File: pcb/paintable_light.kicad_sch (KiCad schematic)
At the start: 19 parts, among them J2 Conn_01x02, J3 Conn_02x03_Odd_Even, U1 WS2811, U2 WS2811, U3 ATtiny85-20P

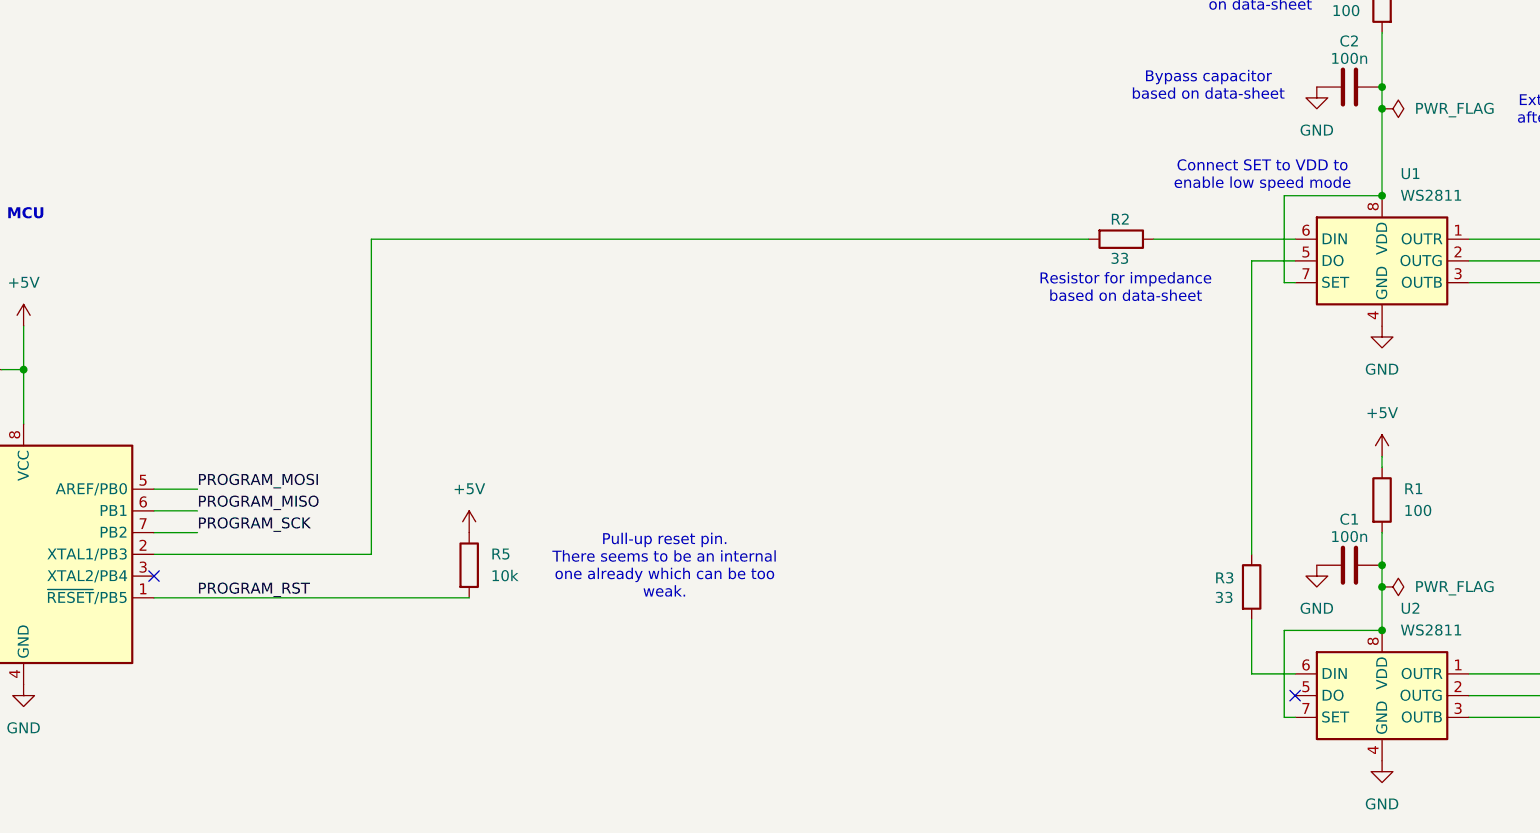
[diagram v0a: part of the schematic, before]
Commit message: enable high speed
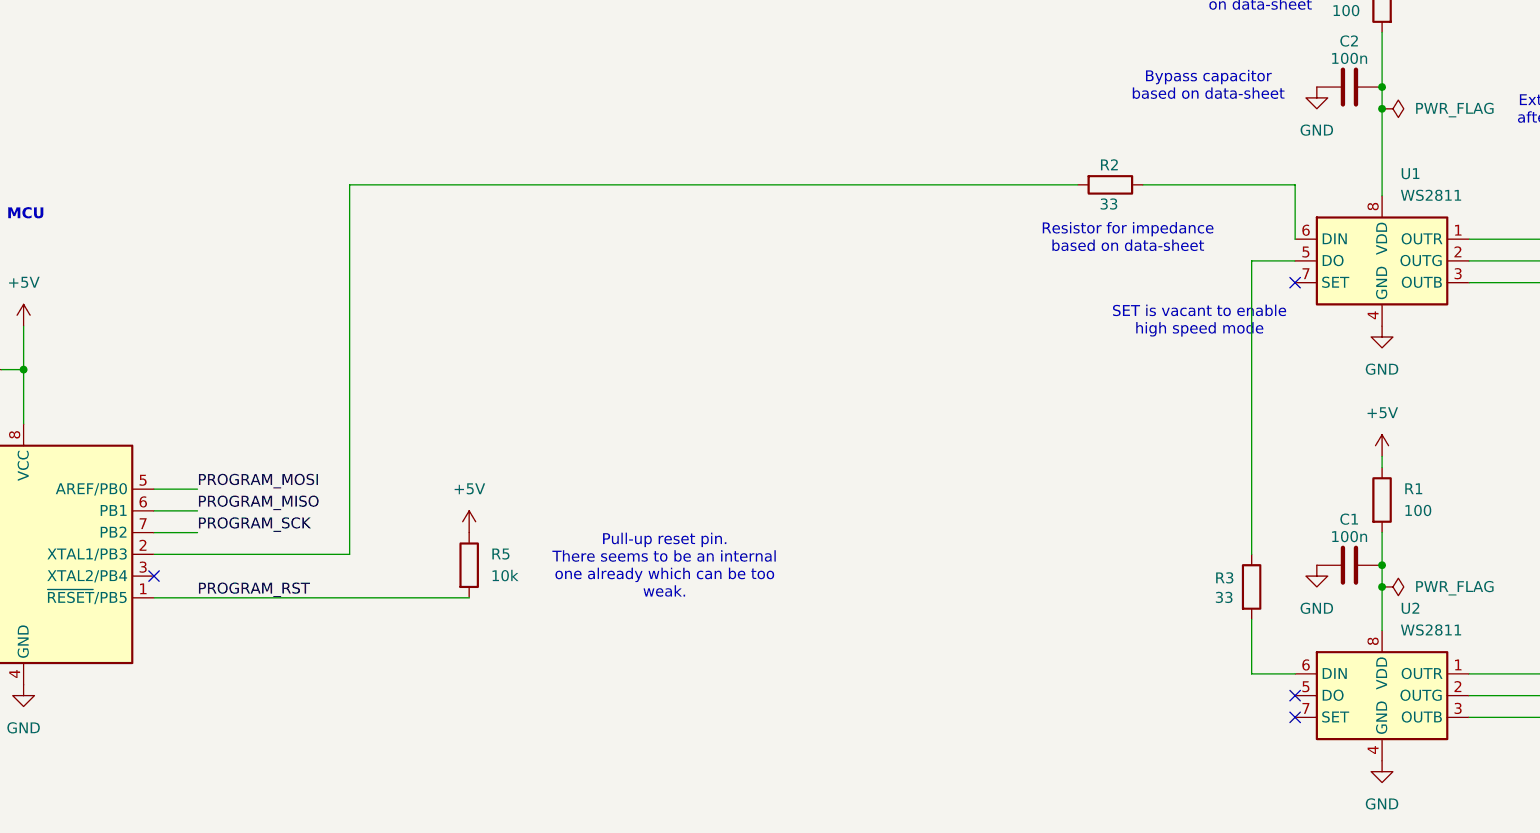
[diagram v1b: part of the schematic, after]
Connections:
- net at C2.2, R4.2, U1.8 (VDD): no longer U1.7 (SET)
- net at C1.2, R1.2, U2.8 (VDD): no longer U2.7 (SET)
- no-connect marks 2 -> 4
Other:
- note added: "SET is vacant to enable high speed mode"
- note removed: "Connect SET to VDD to enable low speed mode"
- moved on the sheet: R2
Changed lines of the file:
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@@
 		)
 	)
-	(text "Bypass capacitor"
+	(text "SET is vacant to enable\nhigh speed mode"
 		(exclude_from_sim no)
-		(at 40.132 98.552 0)
+		(at 195.834 94.742 0)
 		(effects
 			(font
@@
 		)
 	)
-	(text "MCU"
+	(text "Bypass capacitor"
 		(exclude_from_sim no)
-		(at 58.674 82.296 0)
+		(at 40.132 98.552 0)
 		(effects
 			(font
 				(size 1.27 1.27)
-				(thickness 0.254)
-				(bold yes)
 			)
 		)
 	)
-	(text "Resistor for impedance\nbased on data-sheet"
+	(text "MCU"
 		(exclude_from_sim no)
-		(at 187.198 90.932 0)
+		(at 58.674 82.296 0)
 		(effects
 			(font
 				(size 1.27 1.27)
+				(thickness 0.254)
+				(bold yes)
 			)
 		)
 	)
-	(text "Connect SET to VDD to \nenable low speed mode"
+	(text "Resistor for impedance\nbased on data-sheet"
 		(exclude_from_sim no)
-		(at 203.2 77.724 0)
+		(at 187.452 85.09 0)
 		(effects
 			(font
@@
 	)
 	(junction
-		(at 217.17 130.81)
-		(diameter 0)
-		(color 0 0 0 0)
-	)
-	(junction
 		(at 217.17 69.85)
 		(diameter 0)
@@
 	)
 	(junction
-		(at 217.17 80.01)
-		(diameter 0)
-		(color 0 0 0 0)
-	)
-	(junction
 		(at 80.01 34.29)
 		(diameter 0)
@@
 	)
 	(no_connect
+		(at 207.01 140.97)
+	)
+	(no_connect
 		(at 207.01 138.43)
 	)
@@
 		(at 73.66 124.46)
 	)
+	(no_connect
+		(at 207.01 90.17)
+	)
 	(wire
 		(pts
@@
 	(wire
 		(pts
-			(xy 217.17 50.8) (xy 217.17 53.34)
+			(xy 207.01 78.74) (xy 207.01 85.09)
 		)
 		(stroke
@@
 	(wire
 		(pts
-			(xy 73.66 121.92) (xy 99.06 121.92)
+			(xy 189.23 78.74) (xy 207.01 78.74)
 		)
 		(stroke
@@
 	(wire
 		(pts
-			(xy 58.42 95.25) (xy 58.42 100.33)
+			(xy 217.17 50.8) (xy 217.17 53.34)
 		)
 		(stroke
@@
 	(wire
 		(pts
-			(xy 236.22 82.55) (xy 241.3 82.55)
+			(xy 73.66 121.92) (xy 96.52 121.92)
 		)
 		(stroke
@@
 	(wire
 		(pts
-			(xy 99.06 121.92) (xy 99.06 85.09)
+			(xy 58.42 95.25) (xy 58.42 100.33)
 		)
 		(stroke
@@
 	(wire
 		(pts
-			(xy 236.22 143.51) (xy 236.22 140.97)
+			(xy 236.22 82.55) (xy 241.3 82.55)
 		)
 		(stroke
@@
 	(wire
 		(pts
-			(xy 217.17 67.31) (xy 217.17 69.85)
+			(xy 96.52 121.92) (xy 96.52 78.74)
 		)
 		(stroke
@@
 	(wire
 		(pts
-			(xy 58.42 100.33) (xy 58.42 106.68)
+			(xy 236.22 143.51) (xy 236.22 140.97)
 		)
 		(stroke
@@
 	(wire
 		(pts
-			(xy 248.92 143.51) (xy 257.81 143.51)
+			(xy 217.17 67.31) (xy 217.17 69.85)
 		)
 		(stroke
@@
 	(wire
 		(pts
-			(xy 248.92 82.55) (xy 257.81 82.55)
+			(xy 58.42 100.33) (xy 58.42 106.68)
 		)
 		(stroke
@@
 	(wire
 		(pts
-			(xy 201.93 129.54) (xy 201.93 135.89)
+			(xy 248.92 143.51) (xy 257.81 143.51)
 		)
 		(stroke
@@
 	(wire
 		(pts
-			(xy 201.93 87.63) (xy 201.93 121.92)
+			(xy 248.92 82.55) (xy 257.81 82.55)
 		)
 		(stroke
@@
 	(wire
 		(pts
-			(xy 257.81 82.55) (xy 257.81 87.63)
+			(xy 201.93 129.54) (xy 201.93 135.89)
 		)
 		(stroke
@@
 	(wire
 		(pts
-			(xy 207.01 140.97) (xy 205.74 140.97)
+			(xy 201.93 87.63) (xy 201.93 121.92)
 		)
 		(stroke
@@
 	(wire
 		(pts
-			(xy 205.74 80.01) (xy 217.17 80.01)
+			(xy 257.81 82.55) (xy 257.81 87.63)
 		)
 		(stroke
@@
 	(wire
 		(pts
-			(xy 205.74 130.81) (xy 217.17 130.81)
-		)
-		(stroke
-			(width 0)
-			(type default)
-		)
-	)
-	(wire
-		(pts
 			(xy 236.22 85.09) (xy 236.22 82.55)
 		)
@@
 	(wire
 		(pts
-			(xy 99.06 85.09) (xy 182.88 85.09)
+			(xy 96.52 78.74) (xy 181.61 78.74)
 		)
 		(stroke
@@
 	(wire
 		(pts
-			(xy 207.01 90.17) (xy 205.74 90.17)
-		)
-		(stroke
-			(width 0)
-			(type default)
-		)
-	)
-	(wire
-		(pts
 			(xy 80.01 36.83) (xy 80.01 34.29)
 		)
@@
 	(wire
 		(pts
-			(xy 205.74 90.17) (xy 205.74 80.01)
-		)
-		(stroke
-			(width 0)
-			(type default)
-		)
-	)
-	(wire
-		(pts
 			(xy 80.01 31.75) (xy 62.23 31.75)
 		)
@@
 	(wire
 		(pts
-			(xy 205.74 140.97) (xy 205.74 130.81)
-		)
-		(stroke
-			(width 0)
-			(type default)
-		)
-	)
-	(wire
-		(pts
 			(xy 73.66 116.84) (xy 78.74 116.84)
 		)
@@
 	(wire
 		(pts
-			(xy 190.5 85.09) (xy 207.01 85.09)
-		)
-		(stroke
-			(width 0)
-			(type default)
-		)
-	)
-	(wire
-		(pts
 			(xy 227.33 138.43) (xy 241.3 138.43)
 		)
@@
 	(symbol
 		(lib_id "Device:R")
-		(at 186.69 85.09 270)
+		(at 185.42 78.74 270)
 		(unit 1)
 		(exclude_from_sim no)
@@
 		(dnp no)
 		(property "Reference" "R2"
-			(at 185.42 82.804 90)
+			(at 184.15 76.454 90)
 			(effects
 				(font
@@
 		)
 		(property "Value" "33"
-			(at 185.42 87.376 90)
+			(at 184.15 81.026 90)
 			(effects
 				(font
@@
 		)
 		(property "Footprint" "Resistor_SMD:R_0603_1608Metric_Pad0.98x0.95mm_HandSolder"
-			(at 186.69 83.312 90)
+			(at 185.42 76.962 90)
 			(effects
 				(font
@@
 		)
 		(property "Datasheet" "~"
-			(at 186.69 85.09 0)
+			(at 185.42 78.74 0)
 			(effects
 				(font
@@
 		)
 		(property "Description" "Resistor"
-			(at 186.69 85.09 0)
+			(at 185.42 78.74 0)
 			(effects
 				(font

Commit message: initial new board layout
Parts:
- removed J2: Conn_01x02, Connector_PinHeader_2.54mm:PinHeader_1x02_P2.54mm_Vertical, symbol Connector_Generic:Conn_01x02
- removed J3: Conn_02x03_Odd_Even, Connector_PinHeader_2.54mm:PinHeader_2x03_P2.54mm_Vertical, symbol Connector_Generic:Conn_02x03_Odd_Even
- removed U3: ATtiny85-20P, Package_DIP:DIP-8_W7.62mm, symbol MCU_Microchip_ATtiny:ATtiny85-20P
- added C3: 100n, Capacitor_SMD:C_1206_3216Metric_Pad1.33x1.80mm_HandSolder, symbol Device:C
- added D7, D8, D9: LED, LED_SMD:LED_0603_1608Metric_Pad1.05x0.95mm_HandSolder, symbol Device:LED
- added J1: Conn_01x03_Pin, Connector_PinHeader_2.54mm:PinHeader_1x03_P2.54mm_Vertical_SMD_Pin1Left, symbol Connector:Conn_01x03_Pin
- added J2, J3: Conn_01x01, TestPoint:TestPoint_Pad_2.5x2.5mm, symbol Connector_Generic:Conn_01x01
- added R6: 100, Resistor_SMD:R_1206_3216Metric_Pad1.30x1.75mm_HandSolder, symbol Device:R
- added U3: WS2811, Package_SO:SOIC-8_3.9x4.9mm_P1.27mm, symbol Driver_LED:WS2811
- added U4: CH32V003JxMx, Package_SO:JEITA_SOIC-8_3.9x4.9mm_P1.27mm, symbol MCU_WCH_RiscV:CH32V003JxMx
- C1: renamed from C2; footprint Capacitor_SMD:C_0603_1608Metric_Pad1.08x0.95mm_HandSolder -> Capacitor_SMD:C_1206_3216Metric_Pad1.33x1.80mm_HandSolder
- C2: renamed from C1; footprint Capacitor_SMD:C_0603_1608Metric_Pad1.08x0.95mm_HandSolder -> Capacitor_SMD:C_1206_3216Metric_Pad1.33x1.80mm_HandSolder
- C4: renamed from C3; footprint Capacitor_SMD:C_0603_1608Metric_Pad1.08x0.95mm_HandSolder -> Capacitor_SMD:C_1206_3216Metric_Pad1.33x1.80mm_HandSolder
- D1, D2, D3: footprint LED_SMD:LED_0603_1608Metric_Pad1.05x0.95mm_HandSolder -> LED_THT:LED_D5.0mm
- R1: renamed from R2; footprint Resistor_SMD:R_0603_1608Metric_Pad0.98x0.95mm_HandSolder -> Resistor_SMD:R_1206_3216Metric_Pad1.30x1.75mm_HandSolder
- R2: renamed from R4; footprint Resistor_SMD:R_0603_1608Metric_Pad0.98x0.95mm_HandSolder -> Resistor_SMD:R_1206_3216Metric_Pad1.30x1.75mm_HandSolder
- R3: footprint Resistor_SMD:R_0603_1608Metric_Pad0.98x0.95mm_HandSolder -> Resistor_SMD:R_1206_3216Metric_Pad1.30x1.75mm_HandSolder
- R4: renamed from R1; footprint Resistor_SMD:R_0603_1608Metric_Pad0.98x0.95mm_HandSolder -> Resistor_SMD:R_1206_3216Metric_Pad1.30x1.75mm_HandSolder
- R5: value 10k -> 33; footprint Resistor_SMD:R_0603_1608Metric_Pad0.98x0.95mm_HandSolder -> Resistor_SMD:R_1206_3216Metric_Pad1.30x1.75mm_HandSolder
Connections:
- net +5V: now also D7.2 (A), D8.2 (A), D9.2 (A), J1.1 (Pin_1), J2.1 (Pin_1), R6.1, U4.4 (VDD); no longer R5.1
- net GND: now also C3.1, J1.3 (Pin_3), J3.1 (Pin_1), U3.4 (GND), U4.2 (VSS)
- net at U1.6 (DIN): now also R1.2; no longer R1.1
- net at U2.5 (DO): now also R5.1
- net PROGRAM_RST: no longer names the net of R5.2
- net PROGRAM_RST: now also U3.6 (DIN)
- new net: D7.1 (K), U3.1 (OUTR)
- new net: D8.1 (K), U3.2 (OUTG)
- new net: D9.1 (K), U3.3 (OUTB)
- new net: C3.2, R6.2, U3.8 (VDD)
- new net LED Signal: R1.1, U4.5 (PC1)
- new net SWDIO: J1.2 (Pin_2), U4.8 (PD1/PD4/PD5)
- no-connect marks 4 -> 8
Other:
- note added: "0603 LEDs"
- note added: "1210 LEDs"
- note added: "Power supply and programming"
- note added: "Solder pads for power"
- note added: "Through hole LEDs"
- note removed: "Connector for programming the MCU"
- note removed: "Pull-up reset pin. There seems to be an internal one already which can be too weak."
- note removed: "Standard Power Supply"
- moved on the sheet: C1, C2, C4, D1, D2, D3, D4, D5, D6, R1, R2, R3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

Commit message: progress
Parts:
- D1, D2, D3: footprint LED_THT:LED_D5.0mm -> front_leds:LED_1210_3225Metric_Pad1.42x2.65mm_HandSolder_front
- D4, D5, D6: footprint LED_SMD:LED_1210_3225Metric_Pad1.42x2.65mm_HandSolder -> front_leds:LED_1210_3225Metric_Pad1.42x2.65mm_HandSolder_front
- D7, D8, D9: footprint LED_SMD:LED_0603_1608Metric_Pad1.05x0.95mm_HandSolder -> front_leds:LED_1210_3225Metric_Pad1.42x2.65mm_HandSolder_front
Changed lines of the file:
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@@
 			)
 		)
-		(property "Footprint" "LED_SMD:LED_0603_1608Metric_Pad1.05x0.95mm_HandSolder"
+		(property "Footprint" "front_leds:LED_1210_3225Metric_Pad1.42x2.65mm_HandSolder_front"
 			(at 156.21 157.48 0)
 			(effects
@@
 			)
 		)
-		(property "Footprint" "LED_SMD:LED_1210_3225Metric_Pad1.42x2.65mm_HandSolder"
+		(property "Footprint" "front_leds:LED_1210_3225Metric_Pad1.42x2.65mm_HandSolder_front"
 			(at 156.21 116.84 0)
 			(effects
@@
 			)
 		)
-		(property "Footprint" "LED_THT:LED_D5.0mm"
+		(property "Footprint" "front_leds:LED_1210_3225Metric_Pad1.42x2.65mm_HandSolder_front"
 			(at 156.21 66.04 0)
 			(effects
@@
 			)
 		)
-		(property "Footprint" "LED_THT:LED_D5.0mm"
+		(property "Footprint" "front_leds:LED_1210_3225Metric_Pad1.42x2.65mm_HandSolder_front"
 			(at 156.21 71.12 0)
 			(effects
@@
 			)
 		)
-		(property "Footprint" "LED_THT:LED_D5.0mm"
+		(property "Footprint" "front_leds:LED_1210_3225Metric_Pad1.42x2.65mm_HandSolder_front"
 			(at 156.21 76.2 0)
 			(effects
@@
 			)
 		)
-		(property "Footprint" "LED_SMD:LED_1210_3225Metric_Pad1.42x2.65mm_HandSolder"
+		(property "Footprint" "front_leds:LED_1210_3225Metric_Pad1.42x2.65mm_HandSolder_front"
 			(at 156.21 111.76 0)
 			(effects
@@
 			)
 		)
-		(property "Footprint" "LED_SMD:LED_0603_1608Metric_Pad1.05x0.95mm_HandSolder"
+		(property "Footprint" "front_leds:LED_1210_3225Metric_Pad1.42x2.65mm_HandSolder_front"
 			(at 156.21 167.64 0)
 			(effects
@@
 			)
 		)
-		(property "Footprint" "LED_SMD:LED_0603_1608Metric_Pad1.05x0.95mm_HandSolder"
+		(property "Footprint" "front_leds:LED_1210_3225Metric_Pad1.42x2.65mm_HandSolder_front"
 			(at 156.21 162.56 0)
 			(effects
@@
 			)
 		)
-		(property "Footprint" "LED_SMD:LED_1210_3225Metric_Pad1.42x2.65mm_HandSolder"
+		(property "Footprint" "front_leds:LED_1210_3225Metric_Pad1.42x2.65mm_HandSolder_front"
 			(at 156.21 121.92 0)
 			(effects

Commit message: progress
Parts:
- removed J1: Conn_01x03_Pin, Connector_PinHeader_2.54mm:PinHeader_1x03_P2.54mm_Vertical_SMD_Pin1Left, symbol Connector:Conn_01x03_Pin
- added J1: USB_C_Receptacle_PowerOnly_6P, front_leds:vertical_usb_c, symbol Connector:USB_C_Receptacle_PowerOnly_6P
- added J4: Conn_01x01, TestPoint:TestPoint_Pad_2.5x2.5mm, symbol Connector_Generic:Conn_01x01
- added R7, R8: 5k1, Resistor_SMD:R_1206_3216Metric_Pad1.30x1.75mm_HandSolder, symbol Device:R
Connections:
- net +5V: now also J1.A9 (VBUS), J1.B9 (VBUS)
- net GND: now also J1.A12 (GND), J1.B12 (GND), R7.2, R8.2
- net SWDIO: now also J4.1 (Pin_1)
- new net: J1.A5 (CC1), R8.1
- new net: J1.B5 (CC2), R7.1
- no-connect marks 8 -> 9
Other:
- note added: "Solder pads for power and programming"
- note added: "USB Power Supply"
- note removed: "Power supply and programming"
- note removed: "Solder pads for power"
- moved on the sheet: C1, C2, C3, C4, D1, D2, D3, D4, D5, D6, D7, D8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
